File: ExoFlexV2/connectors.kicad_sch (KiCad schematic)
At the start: 12 parts, among them J10 Conn_01x03_Male, J11 Conn_01x05_Male, J12 Conn_01x03_Male, J13 Conn_01x05_Male, J14 Conn_01x03_Male, J15 Conn_01x04_Male, J16 Conn_01x09_Male, J17 Conn_01x08_Male, J18 Conn_01x04_Male, J19 Conn_01x09_Male, J8 Conn_01x03_Male, J9 Conn_01x05_Male

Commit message: quque truc
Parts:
- added D10, D11, D12, D13, D14, D15, D16, D17, D18, D19, D20, D21, D22, D23, D24, D25, D26, D27, D28, D29, D3, D30, D31, D32, D33, D34, D35, D36, D37, D38, D39, D4, D40, D41, D42, D43, D44, D45, D46, D47, D48, D49, D5, D50, D51, D52, D53, D54, D55, D56, D57, D58, D59, D6, D60, D61, D62, D63, D7, D8, D9: TPD1E, FootPrint:DPY2_TEX, symbol Device:D_Zener
- J12: renamed from J9; footprint (none) -> Connector_PinHeader_2.54mm:PinHeader_1x05_P2.54mm_Vertical
- J13: renamed from J11; footprint (none) -> Connector_PinHeader_2.54mm:PinHeader_1x05_P2.54mm_Vertical
- J14: renamed from J13; footprint (none) -> Connector_PinHeader_2.54mm:PinHeader_1x05_P2.54mm_Vertical
- renumbered J12 to J10, J14 to J11, J18 to J16, J16 to J18, J10 to J9
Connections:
- net GND is gone; now on net +5VA: J10.3 (Pin_3), J11.3 (Pin_3), J12.3 (Pin_3), J12.5 (Pin_5), J13.3 (Pin_3), J13.5 (Pin_5), J14.3 (Pin_3), J14.5 (Pin_5), J8.3 (Pin_3), J9.3 (Pin_3)
- net +5VA: now also D10.1 (K), D10.2 (A), D11.1 (K), D11.2 (A), D12.2 (A), D13.1 (K), D13.2 (A), D14.1 (K), D14.2 (A), D15.2 (A), D16.1 (K), D16.2 (A), D17.2 (A), D18.1 (K), D18.2 (A), D19.2 (A), D20.2 (A), D21.2 (A), D22.1 (K), D22.2 (A), D23.2 (A), D24.1 (K), D24.2 (A), D25.1 (K), D25.2 (A), D26.2 (A), D27.1 (K), D27.2 (A), D28.2 (A), D29.2 (A), D3.1 (K), D3.2 (A), D30.1 (K), D30.2 (A), D31.1 (K), D31.2 (A), D32.2 (A), D33.1 (K), D33.2 (A), D38.2 (A), D39.2 (A), D4.1 (K), D4.2 (A), D40.2 (A), D41.2 (A), D42.2 (A), D43.2 (A), D44.2 (A), D45.2 (A), D46.2 (A), D47.2 (A), D48.2 (A), D49.2 (A), D5.2 (A), D50.2 (A), D51.2 (A), D52.2 (A), D53.2 (A), D54.2 (A), D55.2 (A), D56.2 (A), D57.2 (A), D58.2 (A), D59.2 (A), D6.2 (A), D60.2 (A), D61.2 (A), D62.2 (A), D63.2 (A), D7.1 (K), D7.2 (A), D8.1 (K), D8.2 (A), D9.2 (A)
- net BUT_PROX_1: now also D54.1 (K)
- net BUT_PROX_2: now also D51.1 (K)
- net LC1_POT1: now also D62.1 (K)
- net LC1_POT2: now also D56.1 (K)
- net LC1_POT_OUT: now also D59.1 (K)
- net LC2_POT1: now also D53.1 (K)
- net LC2_POT2: now also D47.1 (K)
- net LC2_POT_OUT: now also D50.1 (K)
- net LC3_POT1: now also D44.1 (K)
- net LC3_POT2: now also D39.1 (K)
- net LC3_POT_OUT: now also D41.1 (K)
- net LC_O+_1: now also D32.1 (K)
- net LC_O+_2: now also D21.1 (K)
- net LC_O+_3: now also D9.1 (K)
- net LC_O-_1: now also D29.1 (K)
- net LC_O-_2: now also D15.1 (K)
- net LC_O-_3: now also D5.1 (K)
- net MAG1_POT1: now also D61.1 (K)
- net MAG1_POT2: now also D55.1 (K)
- net MAG1_POT_OUT: now also D58.1 (K)
- net MAG2_POT1: now also D52.1 (K)
- net MAG2_POT2: now also D46.1 (K)
- net MAG2_POT_OUT: now also D49.1 (K)
- net MAG3_POT1: now also D43.1 (K)
- net MAG3_POT2: now also D38.1 (K)
- net MAG3_POT_OUT: now also D40.1 (K)
- net MAG_OUT_1: now also D28.1 (K)
- net MAG_OUT_2: now also D19.1 (K)
- net MAG_OUT_3: now also D12.1 (K)
- net MAG_OUT_4: now also D6.1 (K)
- net PROX_OUT_1: now also D48.1 (K)
- net PROX_OUT_2: now also D45.1 (K)
- net PROX_OUT_3: now also D42.1 (K)
- net RESET: now also D57.1 (K)
- net SWOUT1: now also D26.1 (K)
- net SWOUT2: now also D23.1 (K)
- net SWOUT3: now also D20.1 (K)
- net SWOUT4: now also D17.1 (K)
- net SWOUT5: now also D37.1 (K)
- net SWOUT6: now also D36.1 (K)
- net SWOUT7: now also D35.1 (K)
- net SWOUT8: now also D34.1 (K)
- net URG_USER_1: now also D63.1 (K)
- net URG_USER_2: now also D60.1 (K)
- new net: D34.2 (A), D35.2 (A), D36.2 (A), D37.2 (A)
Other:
- moved on the sheet: J10, J11, J12, J13, J14, J15, J16, J17, J18, J19, J8, J9

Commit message: Placement
Début du placement et modification d'après dernier review
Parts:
- removed D17, D20, D23, D26, D34, D35, D36, D37: TPD1E, FootPrint:DPY2_TEX, symbol Device:D_Zener
- removed J15, J16: Conn_01x04_Male, Connector_PinHeader_2.54mm:PinHeader_1x04_P2.54mm_Vertical, symbol Connector:Conn_01x04_Male
- added D41, D43, D45, D51, D53, D55, D57, D58, D60, D61, D63, D64, D66, D68: TPD1E, FootPrint:DPY2_TEX, symbol Device:D_Zener
- added J17: TOR2, Connector_PinHeader_2.54mm:PinHeader_1x03_P2.54mm_Vertical, symbol Connector:Conn_01x03_Male
- added J18: LIMITSWITCH, Connector_PinHeader_2.54mm:PinHeader_1x08_P2.54mm_Vertical, symbol Connector:Conn_01x08_Male
- added J20: AMP2, Connector_PinHeader_2.54mm:PinHeader_1x03_P2.54mm_Vertical, symbol Connector:Conn_01x03_Male
- J10: value Conn_01x03_Male -> AMP_EVE1
- J11: value Conn_01x03_Male -> SWIVEL
- J12: value Conn_01x05_Male -> TOR_EXT1
- J13: value Conn_01x05_Male -> TOR_DOR1
- J14: value Conn_01x05_Male -> TOR_EVE1
- J15: renamed from J19; value Conn_01x09_Male -> TOR_LIM
- J16: renamed from J18; value Conn_01x09_Male -> AMP_LIM
- J19: renamed from J17; value Conn_01x08_Male -> PROXIMITY
- J8: value Conn_01x03_Male -> AMP_EXT1
- J9: value Conn_01x03_Male -> AMP_DOR1
- renumbered D12 to D10, D9 to D11, D14 to D12, D11 to D13, D39 to D14, D16 to D15, D13 to D16, D41 to D17, D19 to D18, D15 to D19, D44 to D20, D22 to D21, D18 to D22, D47 to D23, D25 to D24, D21 to D25, D50 to D26, D28 to D27, D24 to D28, D53 to D29, D4 to D3, D27 to D31, D56 to D32, D29 to D33, D59 to D34, D31 to D35, D62 to D36, D32 to D37, D33 to D38, D38 to D39, D6 to D4, D43 to D42, D46 to D44, D49 to D46, D52 to D47, D55 to D48, D58 to D49, D3 to D5, D61 to D50, D42 to D52, D45 to D54, D48 to D56, D51 to D59, D8 to D6, D54 to D62, D57 to D65, D60 to D67, D63 to D69, D5 to D7, D10 to D8, D7 to D9
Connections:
- net URG_USER_2 is gone; now on net RESET: D67.1 (K), J19.2 (Pin_2)
- net +5VA: no longer D10.2 (A), D11.2 (A), D12.2 (A), D13.2 (A), D14.2 (A), D15.1 (K), D15.2 (A), D16.1 (K), D16.2 (A), D17.2 (A), D18.2 (A), D19.2 (A), D20.2 (A), D21.2 (A), D22.1 (K), D22.2 (A), D23.2 (A), D24.1 (K), D24.2 (A), D25.2 (A), D26.2 (A), D27.2 (A), D28.2 (A), D29.2 (A), D3.1 (K), D3.2 (A), D30.2 (A), D31.1 (K), D31.2 (A), D32.2 (A), D33.2 (A), D34.2 (A), D35.1 (K), D35.2 (A), D36.2 (A), D37.2 (A), D38.2 (A), D39.2 (A), D4.2 (A), D40.2 (A), D42.2 (A), D44.2 (A), D46.2 (A), D47.2 (A), D48.2 (A), D49.2 (A), D5.1 (K), D5.2 (A), D50.2 (A), D52.2 (A), D54.2 (A), D56.2 (A), D59.2 (A), D6.2 (A), D62.2 (A), D65.2 (A), D67.2 (A), D69.2 (A), D7.2 (A), D8.1 (K), D8.2 (A), D9.1 (K), D9.2 (A), J10.3 (Pin_3), J11.3 (Pin_3), J12.3 (Pin_3), J12.5 (Pin_5), J13.3 (Pin_3), J13.5 (Pin_5), J14.3 (Pin_3), J14.5 (Pin_5), J8.3 (Pin_3), J9.3 (Pin_3)
- net BUT_PROX_1: now also D65.1 (K), J19.3 (Pin_3); no longer D62.1 (K), J19.4 (Pin_4)
- net BUT_PROX_2: now also D62.1 (K), J19.4 (Pin_4); no longer D59.1 (K), J19.5 (Pin_5)
- net PROX_OUT_1: now also D59.1 (K), J19.5 (Pin_5); no longer D56.1 (K), J19.6 (Pin_6)
- net PROX_OUT_2: now also D56.1 (K), J19.6 (Pin_6); no longer D54.1 (K), J19.7 (Pin_7)
- net PROX_OUT_3: now also D54.1 (K), J19.7 (Pin_7); no longer D52.1 (K), J19.8 (Pin_8)
- net RESET: no longer D65.1 (K), J19.3 (Pin_3)
- new net GND: D10.2 (A), D11.2 (A), D12.2 (A), D13.2 (A), D14.2 (A), D15.1 (K), D15.2 (A), D16.1 (K), D16.2 (A), D17.2 (A), D18.2 (A), D19.2 (A), D20.2 (A), D21.2 (A), D22.1 (K), D22.2 (A), D23.2 (A), D24.1 (K), D24.2 (A), D25.2 (A), D26.2 (A), D27.2 (A), D28.2 (A), D29.2 (A), D3.1 (K), D3.2 (A), D30.2 (A), D31.1 (K), D31.2 (A), D32.2 (A), D33.2 (A), D34.2 (A), D35.1 (K), D35.2 (A), D36.2 (A), D37.2 (A), D38.2 (A), D39.2 (A), D4.2 (A), D40.2 (A), D41.2 (A), D42.2 (A), D43.2 (A), D44.2 (A), D45.2 (A), D46.2 (A), D47.2 (A), D48.2 (A), D49.2 (A), D5.1 (K), D5.2 (A), D50.2 (A), D51.2 (A), D52.2 (A), D53.2 (A), D54.2 (A), D55.2 (A), D56.2 (A), D57.2 (A), D58.2 (A), D59.2 (A), D6.2 (A), D60.2 (A), D61.2 (A), D62.2 (A), D63.2 (A), D64.2 (A), D65.2 (A), D66.2 (A), D67.2 (A), D68.2 (A), D69.2 (A), D7.2 (A), D8.1 (K), D8.2 (A), D9.1 (K), D9.2 (A), J10.3 (Pin_3), J11.3 (Pin_3), J12.3 (Pin_3), J12.5 (Pin_5), J13.3 (Pin_3), J13.5 (Pin_5), J14.3 (Pin_3), J14.5 (Pin_5), J8.3 (Pin_3), J9.3 (Pin_3)
- new net MAX_SW_1: D68.1 (K), J18.1 (Pin_1)
- new net MAX_SW_2: D63.1 (K), J18.3 (Pin_3)
- new net MAX_SW_3: D57.1 (K), J18.5 (Pin_5)
- new net MAX_SW_4: D53.1 (K), J18.7 (Pin_7)
- new net MAX_SW_5: D51.1 (K), J18.8 (Pin_8)
- new net MIN_SW_1: D66.1 (K), J18.2 (Pin_2)
- new net MIN_SW_2: D60.1 (K), J18.4 (Pin_4)
- new net MIN_SW_3: D55.1 (K), J18.6 (Pin_6)
- new net MOT_ENC_OUT_1: D64.1 (K), J20.1 (Pin_1)
- new net MOT_ENC_OUT_2: D61.1 (K), J20.2 (Pin_2)
- new net MOT_ENC_OUT_3: D58.1 (K), J20.3 (Pin_3)
- new net TEMP_1: D52.1 (K), J19.8 (Pin_8)
- new net TOR_MOT_OUT_1: D45.1 (K), J17.1 (Pin_1)
- new net TOR_MOT_OUT_2: D43.1 (K), J17.2 (Pin_2)
- new net TOR_MOT_OUT_3: D41.1 (K), J17.3 (Pin_3)
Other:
- note added: "AMPLITUDE"
- note added: "BOUTON ET SWITCH"
- note added: "TORQUE"
- moved on the sheet: D10, D11, D12, D13, D14, D15, D16, D17, D18, D19, D20, D21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

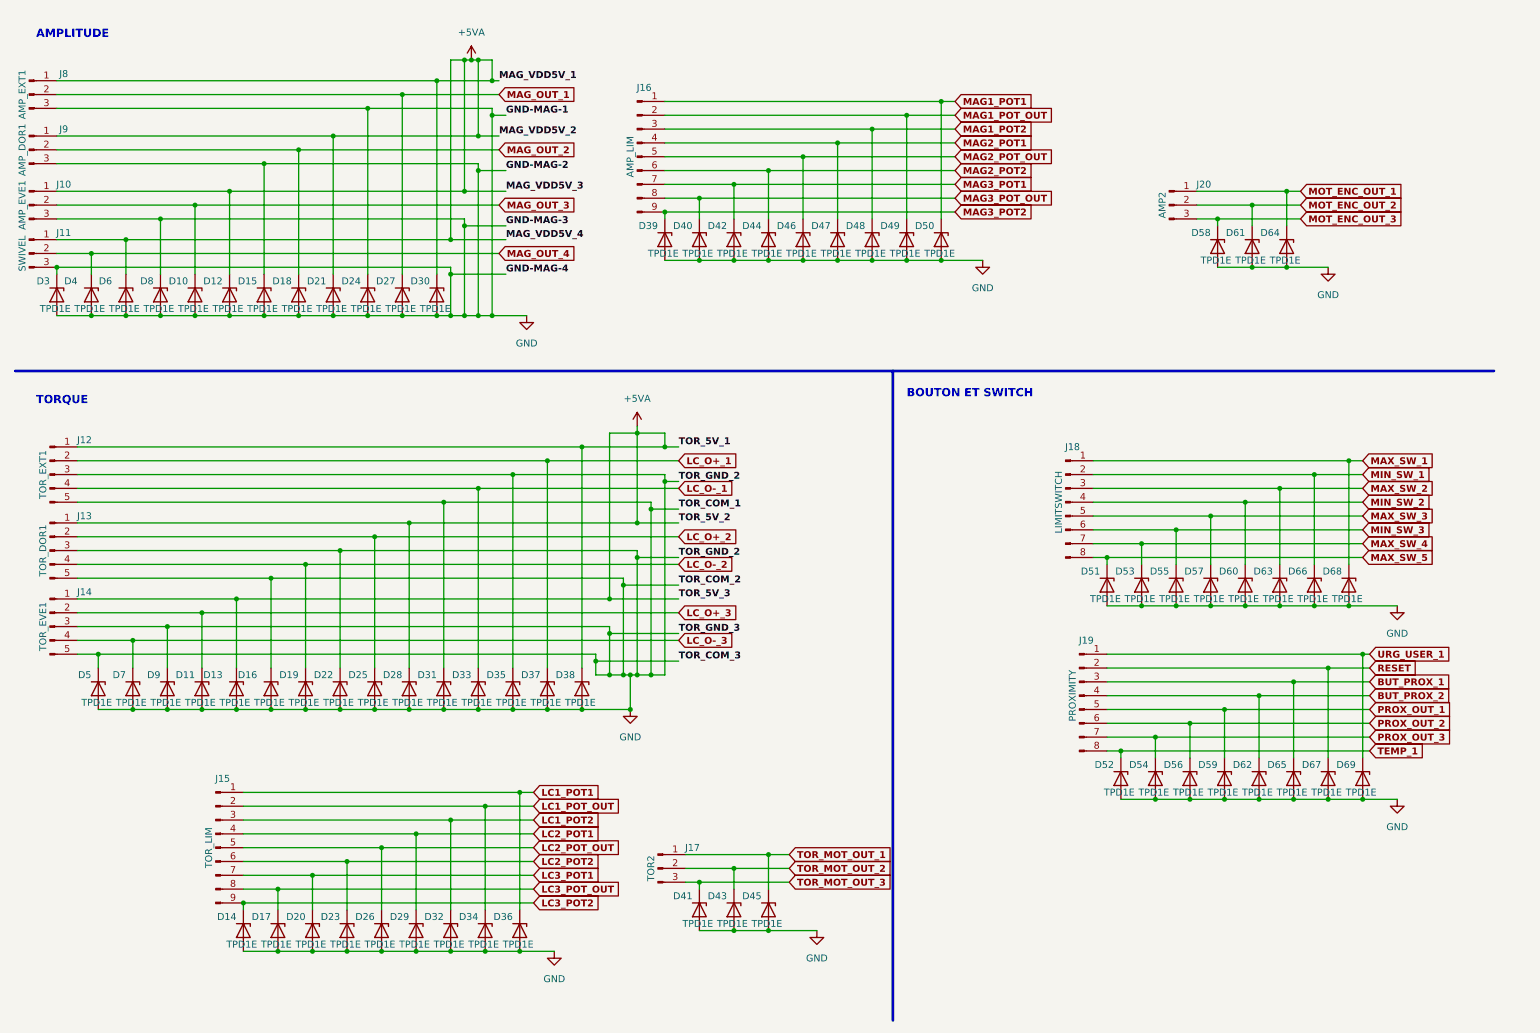
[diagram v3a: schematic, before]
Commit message: Mise à jour mi-stage
- Torque et Amplitude testé et vérifié
- Capteur de présence et de proximité testé
- Système de détection de coupure de fils
- Polyvalence pour plusieurs capteurs
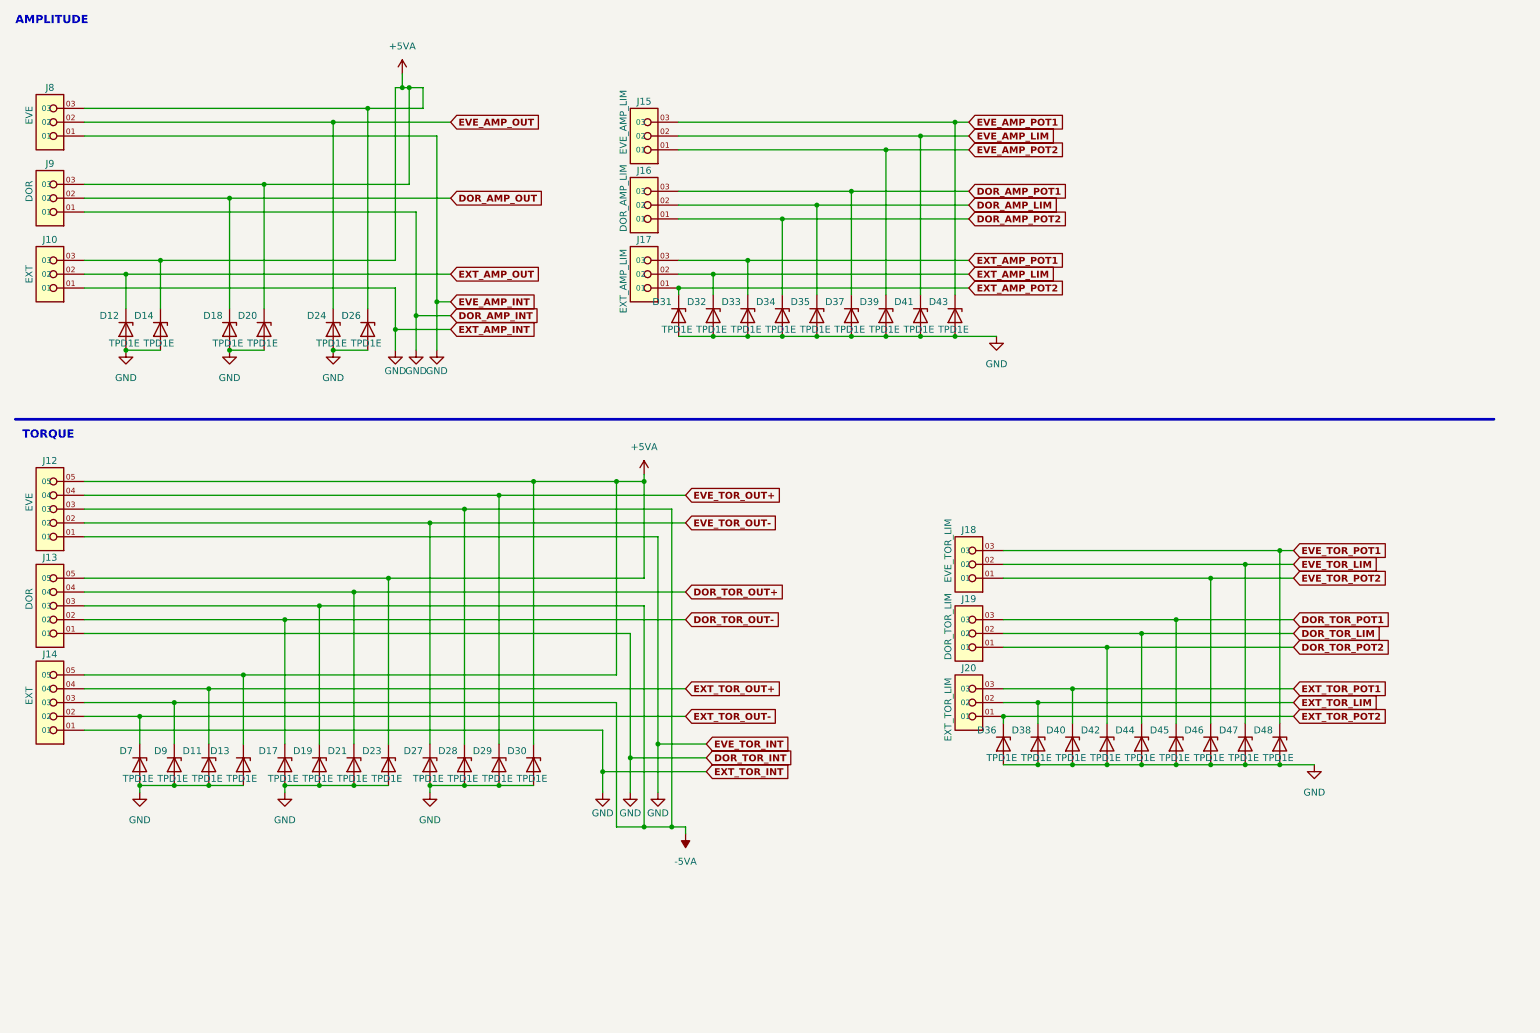
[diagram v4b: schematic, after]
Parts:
- removed D15, D16, D24, D3, D31, D4, D41, D43, D45, D5, D51, D52, D53, D54, D55, D56, D57, D58, D59, D6, D60, D61, D62, D63, D64, D65, D66, D67, D68, D69, D8: TPD1E, FootPrint:DPY2_TEX, symbol Device:D_Zener
- removed J10: AMP_EVE1, Connector_PinHeader_2.54mm:PinHeader_1x03_P2.54mm_Vertical, symbol Connector:Conn_01x03_Male
- removed J11: SWIVEL, Connector_PinHeader_2.54mm:PinHeader_1x03_P2.54mm_Vertical, symbol Connector:Conn_01x03_Male
- removed J12: TOR_EXT1, Connector_PinHeader_2.54mm:PinHeader_1x05_P2.54mm_Vertical, symbol Connector:Conn_01x05_Male
- removed J13: TOR_DOR1, Connector_PinHeader_2.54mm:PinHeader_1x05_P2.54mm_Vertical, symbol Connector:Conn_01x05_Male
- removed J14: TOR_EVE1, Connector_PinHeader_2.54mm:PinHeader_1x05_P2.54mm_Vertical, symbol Connector:Conn_01x05_Male
- removed J15: TOR_LIM, Connector_PinHeader_2.54mm:PinHeader_1x09_P2.54mm_Vertical, symbol Connector:Conn_01x09_Male
- removed J16: AMP_LIM, Connector_PinHeader_2.54mm:PinHeader_1x09_P2.54mm_Vertical, symbol Connector:Conn_01x09_Male
- removed J17: TOR2, Connector_PinHeader_2.54mm:PinHeader_1x03_P2.54mm_Vertical, symbol Connector:Conn_01x03_Male
- removed J18: LIMITSWITCH, Connector_PinHeader_2.54mm:PinHeader_1x08_P2.54mm_Vertical, symbol Connector:Conn_01x08_Male
- removed J19: PROXIMITY, Connector_PinHeader_2.54mm:PinHeader_1x08_P2.54mm_Vertical, symbol Connector:Conn_01x08_Male
- removed J20: AMP2, Connector_PinHeader_2.54mm:PinHeader_1x03_P2.54mm_Vertical, symbol Connector:Conn_01x03_Male
- removed J8: AMP_EXT1, Connector_PinHeader_2.54mm:PinHeader_1x03_P2.54mm_Vertical, symbol Connector:Conn_01x03_Male
- removed J9: AMP_DOR1, Connector_PinHeader_2.54mm:PinHeader_1x03_P2.54mm_Vertical, symbol Connector:Conn_01x03_Male
- added J10: EXT, FootPrint:PHOENIX_1751109, symbol SymLib:1751109
- added J12: EVE, FootPrint:PHOENIX_1751125, symbol SymLib:1751125
- added J13: DOR, FootPrint:PHOENIX_1751125, symbol SymLib:1751125
- added J14: EXT, FootPrint:PHOENIX_1751125, symbol SymLib:1751125
- added J15: EVE_AMP_LIM, FootPrint:PHOENIX_1751109, symbol SymLib:1751109
- added J16: DOR_AMP_LIM, FootPrint:PHOENIX_1751109, symbol SymLib:1751109
- added J17: EXT_AMP_LIM, FootPrint:PHOENIX_1751109, symbol SymLib:1751109
- added J18: EVE_TOR_LIM, FootPrint:PHOENIX_1751109, symbol SymLib:1751109
- added J19: DOR_TOR_LIM, FootPrint:PHOENIX_1751109, symbol SymLib:1751109
- added J20: EXT_TOR_LIM, FootPrint:PHOENIX_1751109, symbol SymLib:1751109
- added J8: EVE, FootPrint:PHOENIX_1751109, symbol SymLib:1751109
- added J9: DOR, FootPrint:PHOENIX_1751109, symbol SymLib:1751109
- renumbered D10 to D12, D12 to D14, D19 to D17, D22 to D19, D21 to D20, D25 to D21, D28 to D23, D27 to D24, D30 to D26, D33 to D27, D35 to D28, D37 to D29, D38 to D30, D39 to D31, D40 to D32, D42 to D33, D44 to D34, D46 to D35, D14 to D36, D47 to D37, D17 to D38, D48 to D39, D20 to D40, D49 to D41, D23 to D42, D50 to D43, D26 to D44, D29 to D45, D32 to D46, D34 to D47, D36 to D48
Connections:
- net +5VA: now also J10.03, J12.05, J13.05, J14.05, J8.03, J9.03
- net GND: now also J10.01, J12.01, J13.01, J14.01, J8.01, J9.01; no longer D19.1 (K), D28.1 (K), D9.1 (K)
- net LC1_POT1 renamed EVE_TOR_POT1
- net EVE_TOR_POT1: now also J18.03
- net LC1_POT2 renamed EVE_TOR_POT2
- net EVE_TOR_POT2: now also J18.01
- net LC1_POT_OUT renamed EVE_TOR_LIM
- net EVE_TOR_LIM: now also J18.02
- net LC2_POT1 renamed DOR_TOR_POT1
- net DOR_TOR_POT1: now also J19.03
- net LC2_POT2 renamed DOR_TOR_POT2
- net DOR_TOR_POT2: now also J19.01
- net LC2_POT_OUT renamed DOR_TOR_LIM
- net DOR_TOR_LIM: now also J19.02
- net LC3_POT1 renamed EXT_TOR_POT1
- net EXT_TOR_POT1: now also J20.03
- net LC3_POT2 renamed EXT_TOR_POT2
- net EXT_TOR_POT2: now also J20.01
- net LC3_POT_OUT renamed EXT_TOR_LIM
- net EXT_TOR_LIM: now also J20.02
- net LC_O+_1 renamed EVE_TOR_OUT+
- net EVE_TOR_OUT+: now also J12.04
- net LC_O+_2 renamed DOR_TOR_OUT+
- net DOR_TOR_OUT+: now also J13.04
- net LC_O+_3 renamed EXT_TOR_OUT+
- net EXT_TOR_OUT+: now also J14.04
- net LC_O-_1 renamed EVE_TOR_OUT-
- net EVE_TOR_OUT-: now also J12.02
- net LC_O-_2 renamed DOR_TOR_OUT-
- net DOR_TOR_OUT-: now also J13.02
- net LC_O-_3 renamed EXT_TOR_OUT-
- net EXT_TOR_OUT-: now also J14.02
- net MAG1_POT1 renamed EVE_AMP_POT1
- net EVE_AMP_POT1: now also J15.03
- net MAG1_POT2 renamed EVE_AMP_POT2
- net EVE_AMP_POT2: now also J15.01
- net MAG1_POT_OUT renamed EVE_AMP_LIM
- net EVE_AMP_LIM: now also J15.02
- net MAG2_POT1 renamed DOR_AMP_POT1
- net DOR_AMP_POT1: now also J16.03
- net MAG2_POT2 renamed DOR_AMP_POT2
- net DOR_AMP_POT2: now also J16.01
- net MAG2_POT_OUT renamed DOR_AMP_LIM
- net DOR_AMP_LIM: now also J16.02
- net MAG3_POT1 renamed EXT_AMP_POT1
- net EXT_AMP_POT1: now also J17.03
- net MAG3_POT2 renamed EXT_AMP_POT2
- net EXT_AMP_POT2: now also J17.01
- net MAG3_POT_OUT renamed EXT_AMP_LIM
- net EXT_AMP_LIM: now also J17.02
- net MAG_OUT_1 renamed EVE_AMP_OUT
- net EVE_AMP_OUT: now also J8.02
- net MAG_OUT_2 renamed DOR_AMP_OUT
- net DOR_AMP_OUT: now also J9.02
- net MAG_OUT_3 renamed EXT_AMP_OUT
- net EXT_AMP_OUT: now also J10.02
- new net -5VA: D19.1 (K), D28.1 (K), D9.1 (K), J12.03, J13.03, J14.03
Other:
- note removed: "BOUTON ET SWITCH"
- moved on the sheet: D11, D12, D13, D14, D17, D18, D19, D20, D21, D23, D24, D26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

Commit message: Mise à jour signaux STM
- Condo de découplage
- Signaux supplémentaire pour le STM
- Page GND sera pour Multiplexeur
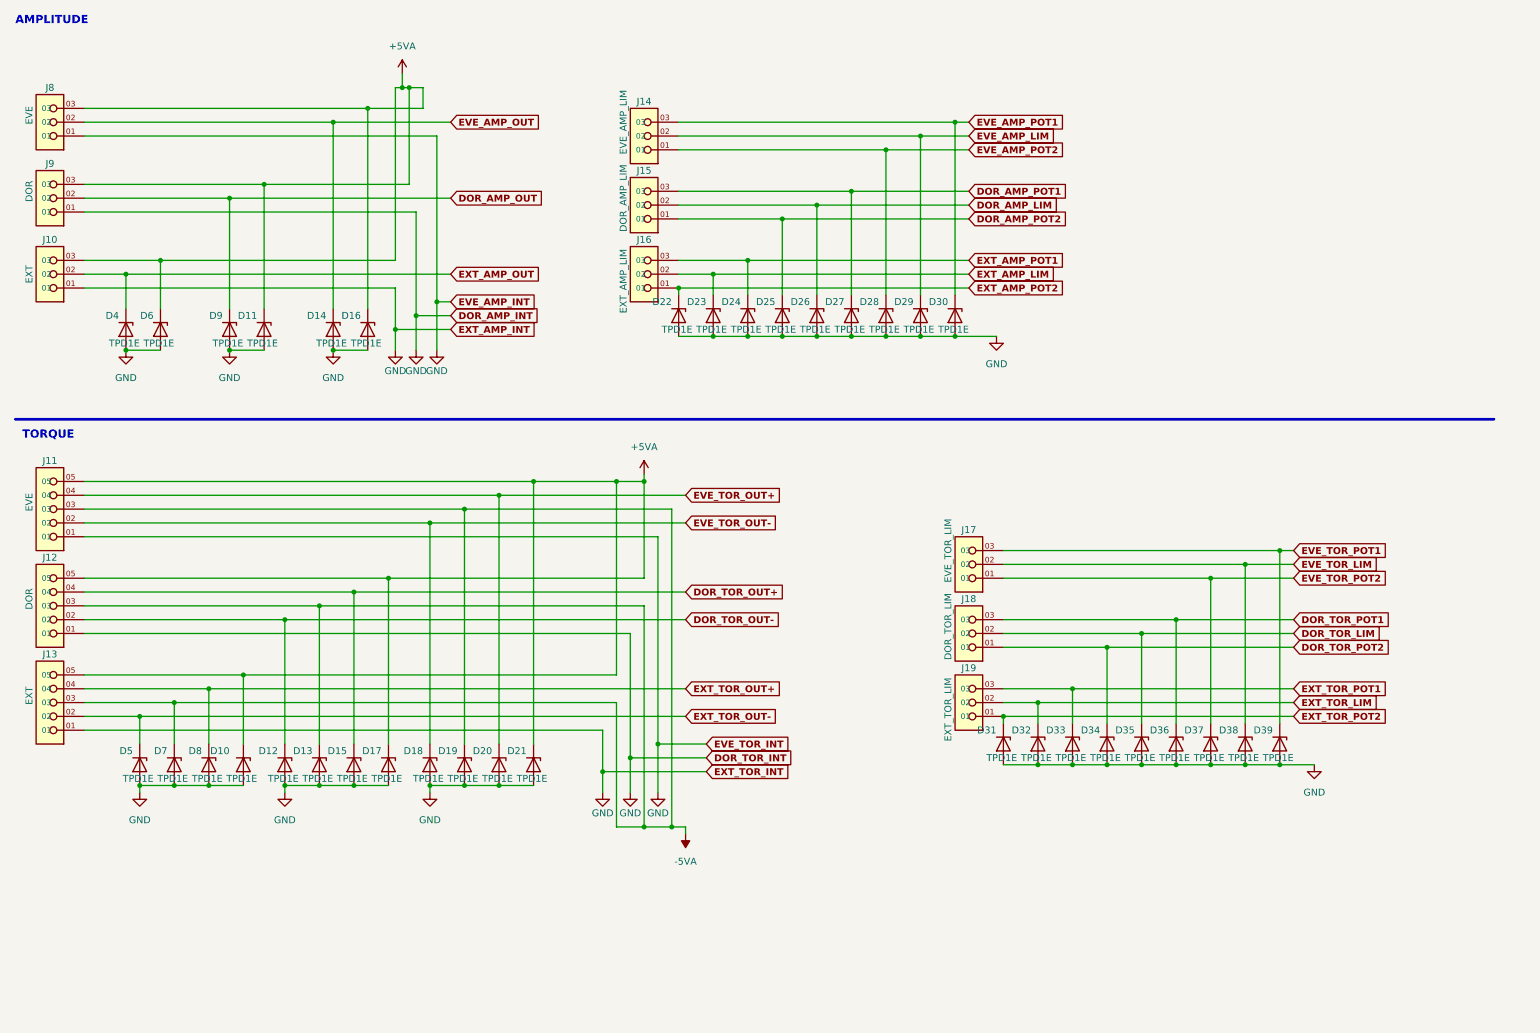
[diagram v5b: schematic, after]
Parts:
- renumbered D13 to D10, D20 to D11, D17 to D12, D19 to D13, D24 to D14, D21 to D15, D26 to D16, D23 to D17, D27 to D18, D28 to D19, D29 to D20, D30 to D21, D31 to D22, D32 to D23, D33 to D24, D34 to D25, D35 to D26, D37 to D27, D39 to D28, D41 to D29, D43 to D30, D36 to D31, D38 to D32, D40 to D33, D42 to D34, D44 to D35, D45 to D36, D46 to D37, D47 to D38, D48 to D39, D12 to D4, D7 to D5, D14 to D6, D9 to D7, D11 to D8, D18 to D9, J12 to J11, J13 to J12, J14 to J13, J15 to J14, J16 to J15, J17 to J16, J18 to J17, J19 to J18, J20 to J19
